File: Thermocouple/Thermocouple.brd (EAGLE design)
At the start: 25.4 x 25.4 mm, 20 parts, among them Q2 BSS138

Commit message: Latest version of schematics and boards
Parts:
- removed C5: 10uF, SparkFun-Capacitors:0805
- removed LED: blue, led:CHIPLED_1206
- removed Q2: BSS138, SparkFun-DiscreteSemi:SOT23
- added C10, C4: 1uF, SparkFun-Capacitors:0805
- added C12, C6, C8, C9: .1uF, SparkFun-Capacitors:0805
- added C7: .47uF, SparkFun-Capacitors:0805
- added JP2: M023.5MM, SparkFun-Connectors:SCREWTERMINAL-3.5MM-2
- added L1: 1mH, SparkFun-Passives:1007
- added LED1: (no value), adafruit:CHIP-LED0805
- added R4: 24k, SparkFun-Resistors:0805
- added TP1, TP2, TP3, TP4, TP5, TP6, TP7, TP8, TP9: TEST-POINT3, SparkFun-Passives:PAD.03X.03
- C1: value .1uF -> .47uF
- C2: value 10uF -> .1uF
- JP1: value (none) -> M023.5MM; device SparkFun-Connectors:SCREWTERMINAL-3.5MM-4 -> SparkFun-Connectors:SCREWTERMINAL-3.5MM-2
- R1: value 1k -> 680; device SparkFun-Resistors:0805 -> SparkFun-Passives:0805
- R2: value 2k -> 1
- R3: value 680 -> 24k; device SparkFun-Passives:0805 -> SparkFun-Resistors:0805
- R5, R8: value 1k -> 1M
- R6: value 2k -> 24k
- R7: value 1k -> 24k
- R9: value 2k -> 22; device SparkFun-Resistors:0805 -> SparkFun-Passives:0805
- U$1: value MAX31855 -> AD8495; device IntegerLabs:SOIC-8 -> IntegerLabs:MSOP-8
- U$2: value MIC5205-3.3 -> FOOTPRINTFOOTPRINT-2; device SparkFun-PowerIC:SOT23-5 -> IntegerLabs:FOOTPRINT2
- U$3: value TINY841 -> ATTINY48/88-TQFP; device IntegerLabs:SOIC14 -> IntegerLabs:TQFP-32
- U$4: value FOOTPRINT -> AD8495; device IntegerLabs:FOOTPRINT -> IntegerLabs:MSOP-8
- U$5: value MAX31855 -> zener; device IntegerLabs:SOIC-8 -> SparkFun-DiscreteSemi:SOD-323
- moved R3 28.3 mm to (31.1, 12.4), turned to 90 degrees
- moved U$4 28.1 mm to (19.7, 20.0), turned to 90 degrees
- moved C2 24.5 mm to (27.3, 15.6), turned to 270 degrees
- moved R5 14.5 mm to (29.2, 12.4), turned to 270 degrees
- moved R6 13.9 mm to (22.9, 12.1), turned to 90 degrees
- moved U$5 13.7 mm to (17.1, 24.1), turned to 270 degrees
- moved C3 13.6 mm to (31.1, 15.6)
- moved JP1 13.3 mm to (22.5, 6.67)
- moved U$2 13.0 mm to (0.00, 0.00), turned to 0 degrees
- moved U$1 11.5 mm to (28.6, 20.3), turned to 90 degrees
- moved R8 10.4 mm to (21.0, 12.1), turned to 270 degrees
- moved R1 9.38 mm to (22.5, 27.9), turned to 90 degrees
- moved R9 9.14 mm to (19.4, 24.1), turned to 90 degrees
- moved U$3 7.96 mm to (8.57, 21.3)
- moved R7 7.81 mm to (19.1, 12.1), turned to 90 degrees
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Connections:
- removed net +3.3V: C3.1, C5.1, U$1.4, U$2.5, U$5.4
- removed net +5V: C1.1, C2.1, R1.2, U$2.1, U$2.3, U$3.1, U$4.P$1
- removed net CS1: R2.2, U$3.2
- removed net CS1-3.3: R2.1, R5.2, U$1.6
- removed net CS2: R6.2, U$3.3
- removed net CS2-3.3: R6.1, R7.2, U$5.6
- removed net MISO3.3: Q2.1, U$1.7, U$5.7
- removed net MISO5: Q2.3, R1.1, U$3.6
- removed net SCK-3.3: R8.2, R9.1, U$1.5, U$5.5
- removed net SCL/SCK: U$3.9, U$4.P$4
- removed net SDA/MOSI: U$3.7, U$4.P$2
- removed net T1+: JP1.4, U$1.3
- removed net T1-: JP1.3, U$1.2
- removed net T2+: JP1.2, U$5.3
- removed net T2-: JP1.1, U$5.2
- new net AVCC: C7.1, L1.1, TP4.P$1, TP5.P$1, U$1.7, U$3.18, U$4.7, U$5.1
- new net IN1+: JP1.1, R4.1, TP6.P$1
- new net IN1-: JP1.2, R3.1, R5.2, TP7.P$1
- new net IN2+: JP2.1, R7.1, TP8.P$1
- new net IN2-: JP2.2, R6.1, R8.2, TP9.P$1
- new net MOSI: U$2.PROG4, U$3.15
- new net N$2: R2.2, U$2.BUS2
- new net N$3: C3.2, C4.1, R3.2, U$1.1
- new net N$4: C2.1, C4.2, R4.2, U$1.8
- new net N$6: C10.2, C8.1, R7.2, U$4.8
- new net N$7: L1.2, R9.1
- new net N$8: LED1.A, R1.1
- new net SCL: U$2.BUS3, U$3.28
- new net SDA: U$2.BUS1, U$3.27
- new net TEMP1: C6.1, TP1.P$1, U$1.5, U$1.6, U$3.3
- new net TEMP2: C12.1, TP2.P$1, U$3.6, U$4.5, U$4.6
- new net VCC: C1.2, R2.1, R9.2, U$2.PROG0, U$3.4
- net GND: now also C1.1, C12.2, C3.1, C6.2, C7.2, C8.2, C9.1, LED1.C, TP3.P$1, U$1.2, U$1.3, U$2.BUS0, U$3.21, U$3.5, U$4.2, U$4.3, U$5.2; no longer C1.2, C3.2, C5.2, LED.C, Q2.2, R7.1, U$1.1, U$2.2, U$3.14, U$4.P$3, U$5.1
- net LED: now also R1.2, U$3.13; no longer R3.2, U$3.12
- net MISO: now also U$2.PROG3, U$3.16; no longer U$3.8, U$4.MISO
- net N$5: now also C10.1, C9.2, R6.2, U$4.1; no longer LED.A, R3.1
- net RESET: now also U$2.PROG1, U$3.29; no longer U$3.4, U$4.RESET
- net SCK: now also U$2.PROG2, U$3.17; no longer R9.2, U$3.5
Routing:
- net VCC: track 0.00 -> 40.9 mm, vias 0 -> 1
- net TEMP1: track 0.00 -> 39.0 mm, vias 0 -> 5
- net +5V: track 37.7 -> 0.00 mm, vias 3 -> 0
- net GND: track 72.3 -> 38.8 mm, vias 5 -> 14
- net AVCC: track 0.00 -> 32.3 mm
- net SCL: track 0.00 -> 25.0 mm, vias 0 -> 1
- net SCK-3.3: track 21.9 -> 0.00 mm, vias 4 -> 0
- net LED: track 10.4 -> 31.9 mm, vias 0 -> 2
- net +3.3V: track 21.2 -> 0.00 mm
- net MOSI: track 0.00 -> 19.5 mm, vias 0 -> 1
- net SCL/SCK: track 19.1 -> 0.00 mm, vias 1 -> 0
- net MISO5: track 18.0 -> 0.00 mm, vias 2 -> 0
- net IN2-: track 0.00 -> 17.9 mm
- net MISO3.3: track 17.2 -> 0.00 mm
- net IN1+: track 0.00 -> 16.1 mm
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- added copper zone on layer 16, net GND
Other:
- board size 25.4 x 25.4 mm -> 35.6 x 29.8 mm
- board text added: "+: yellow"
- board text added: "-"
- board text added: "-: red"
- board text added: "A"
- board text added: "A+"
- board text added: "A-"
- board text added: "B"
- board text added: "B+"
- board text added: "B-"
- board text added: "Modulo"
- board text added: "Thermocouple"
- board text added: "v3 2014-10-10"
- board text removed: "2014-07-03"
- board text removed: "T1+"
- board text removed: "T1-"
- board text removed: "T2+"
- board text removed: "T2-"
- board text removed: "Thermocouple v1"

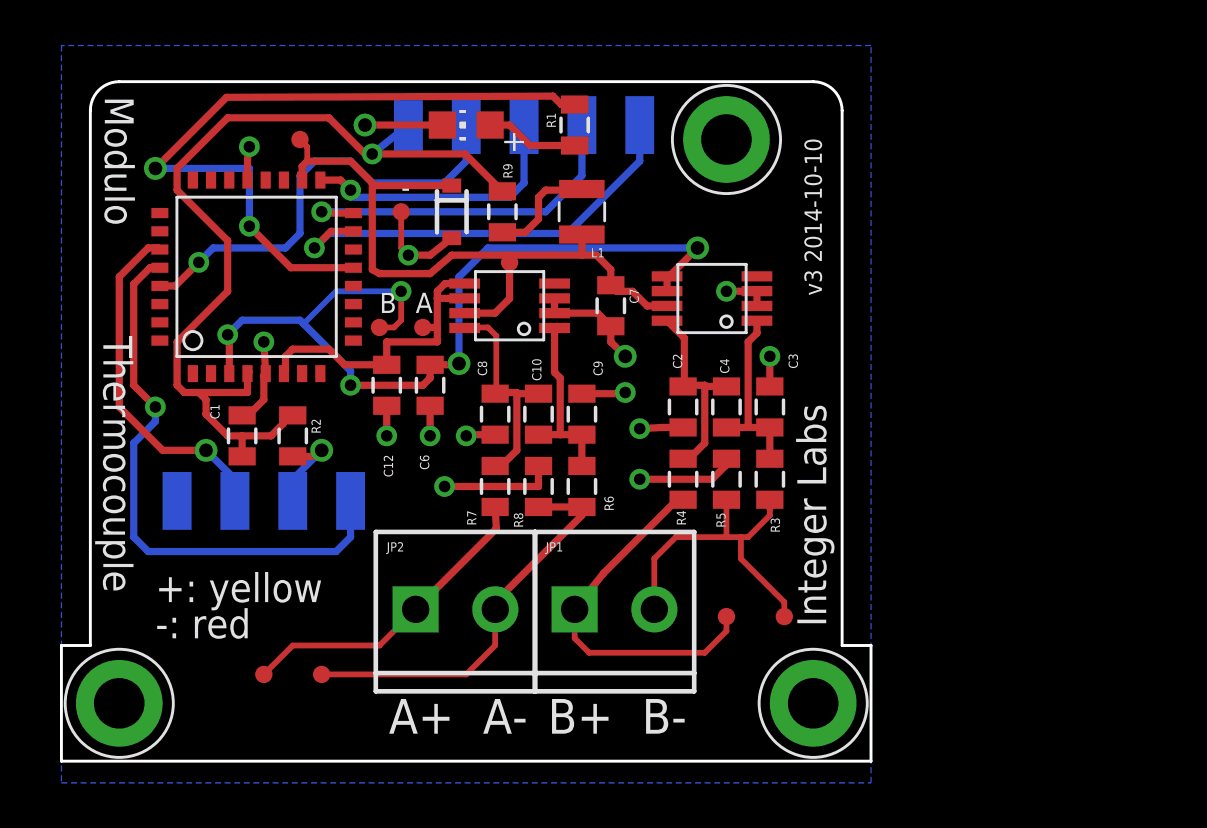
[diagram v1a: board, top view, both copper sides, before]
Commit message: OLED: added buttons and rewired for attiny841 Thermocouple: checkpoint of latest version with two amplifiers and attiny48
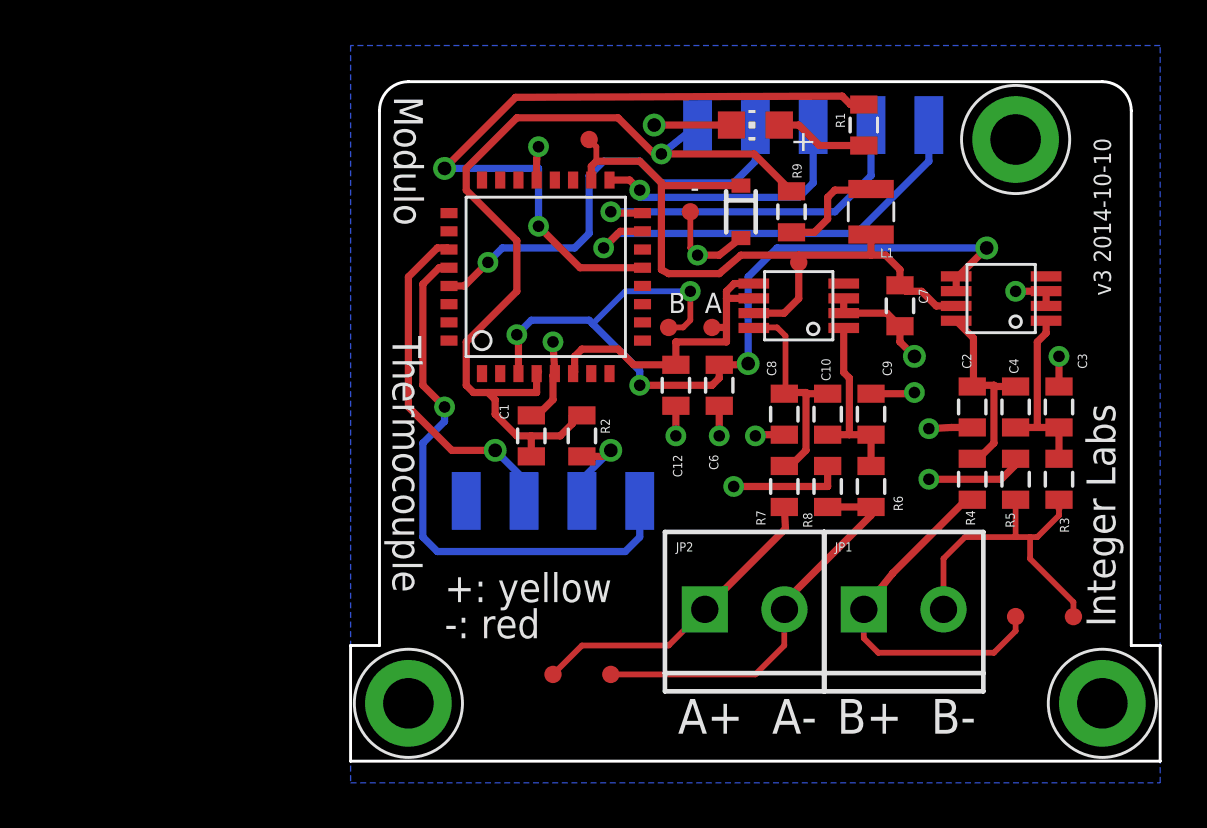
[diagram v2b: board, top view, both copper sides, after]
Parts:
- moved C10 12.7 mm to (33.7, 15.2)
- moved C2 12.7 mm to (40.0, 15.6)
- moved C9 12.7 mm to (35.6, 15.2)
- moved L1 12.7 mm to (35.6, 24.1)
- moved R4 12.7 mm to (40.0, 12.4)
- moved R6 12.7 mm to (35.6, 12.1)
- moved R8 12.7 mm to (33.7, 12.1)
- moved R9 12.7 mm to (32.1, 24.1)
- moved TP7 12.7 mm to (44.5, 6.35)
- moved C12 12.7 mm to (27.0, 16.5)
- moved JP2 12.7 mm to (28.3, 6.67)
- moved TP1 12.7 mm to (26.7, 19.1)
- moved U$3 12.7 mm to (21.3, 21.3)
- moved C1 12.7 mm to (20.6, 14.3)
- moved C3 12.7 mm to (43.8, 15.6)
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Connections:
- net TEMP1 renamed TEMPB
- net TEMP2 renamed TEMPA

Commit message: New thermocouple revision with single input and quick connect terminals
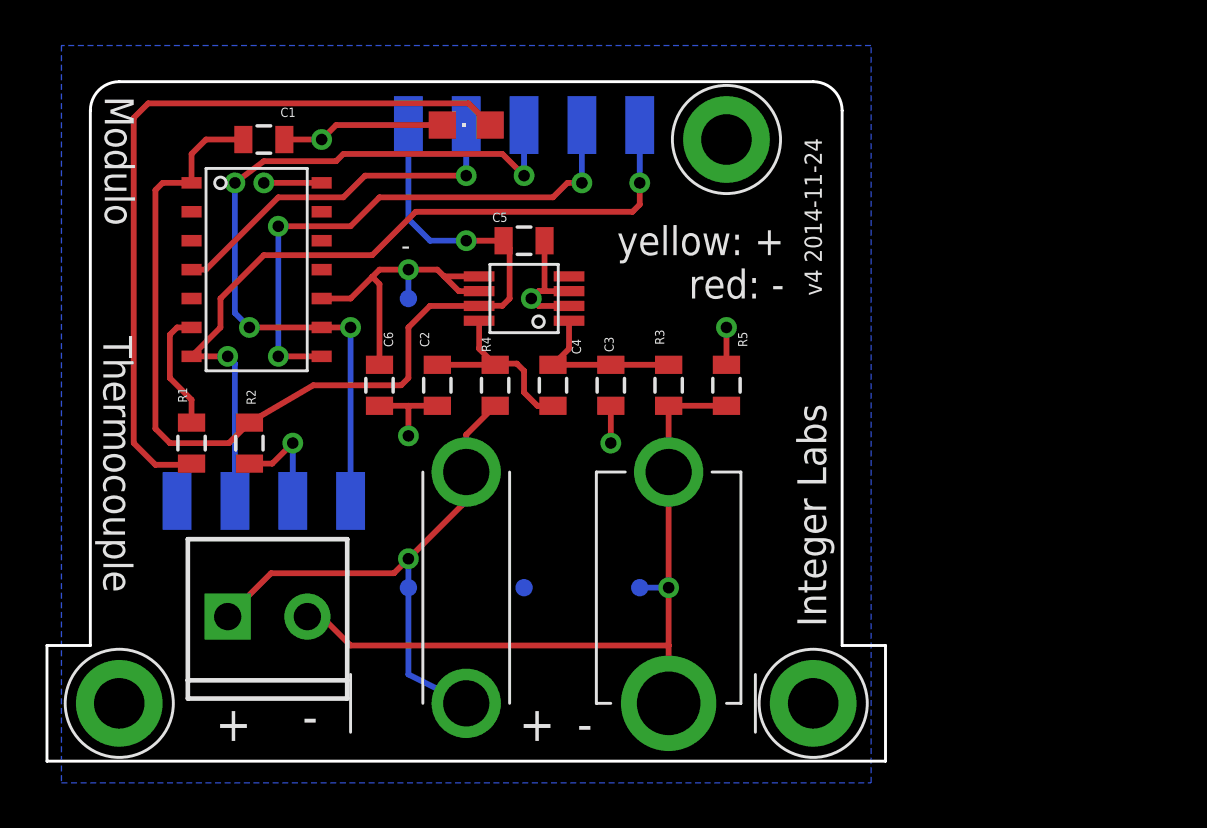
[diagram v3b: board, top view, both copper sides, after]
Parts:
- removed C10: 1uF, SparkFun-Capacitors:0805
- removed C12, C8, C9: .1uF, SparkFun-Capacitors:0805
- removed C7: .47uF, SparkFun-Capacitors:0805
- removed JP2: M023.5MM, SparkFun-Connectors:SCREWTERMINAL-3.5MM-2
- removed L1: 1mH, SparkFun-Passives:1007
- removed R6, R7: 24k, SparkFun-Resistors:0805
- removed R8: 1M, SparkFun-Resistors:0805
- removed R9: 22, SparkFun-Passives:0805
- removed TP1, TP4, TP5, TP8, TP9: TEST-POINT3, SparkFun-Passives:PAD.03X.03
- removed U$5: zener, SparkFun-DiscreteSemi:SOD-323
- added C5: .47uF, SparkFun-Capacitors:0805
- C2, C3, C6: value .1uF -> .47uF
- LED1: device adafruit:CHIP-LED0805 -> adafruit:CHIPLED_0805
- U$3: value ATTINY48/88-TQFP -> TINY841; device IntegerLabs:TQFP-32 -> IntegerLabs:SOIC14
- U$4: value AD8495 -> THERMOCOUPLE-JACK; device IntegerLabs:MSOP-8 -> IntegerLabs:THERMOCOUPLE-JACK
- moved R1 32.7 mm to (5.71, 14.0)
- moved JP1 27.9 mm to (7.30, 6.35)
- moved TP6 26.7 mm to (15.2, 7.62), flipped to the bottom
- moved C2 23.5 mm to (16.5, 16.5)
- moved U$4 22.8 mm to (17.8, 2.54), turned to 0 degrees
- moved R4 21.4 mm to (19.1, 16.5)
- moved U$1 21.0 mm to (20.3, 20.3)
- moved C4 20.3 mm to (21.6, 16.5), turned to 270 degrees
- moved C3 19.7 mm to (24.1, 16.5), turned to 90 degrees
- moved TP7 19.1 mm to (25.4, 7.62), flipped to the bottom
- moved TP3 18.1 mm to (20.3, 7.62), flipped to the bottom
- moved R3 17.6 mm to (26.7, 16.5)
- moved C1 17.5 mm to (8.89, 27.3), turned to 180 degrees
- moved C6 14.9 mm to (14.0, 16.5)
- moved R2 14.6 mm to (8.26, 14.0)
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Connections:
- removed net AVCC: C7.1, L1.1, TP4.P$1, TP5.P$1, U$1.7, U$3.18, U$4.7, U$5.1
- removed net IN2+: JP2.1, R7.1, TP8.P$1
- removed net IN2-: JP2.2, R6.1, R8.2, TP9.P$1
- removed net MOSI: U$2.PROG4, U$3.15
- removed net N$5: C10.1, C9.2, R6.2, U$4.1
- removed net N$6: C10.2, C8.1, R7.2, U$4.8
- removed net N$7: L1.2, R9.1
- removed net SCK: U$2.PROG2, U$3.17
- removed net SCL: U$2.BUS3, U$3.28
- removed net SDA: U$2.BUS1, U$3.27
- removed net TEMPA: C12.1, TP2.P$1, U$3.6, U$4.5, U$4.6
- removed net TEMPB: C6.1, TP1.P$1, U$1.5, U$1.6, U$3.3
- new net SCL/SCK: U$2.BUS3, U$2.PROG2, U$3.9
- new net SDA/MOSI: U$2.BUS1, U$2.PROG4, U$3.7
- new net TEMP: C6.1, TP2.P$1, U$1.5, U$1.6, U$3.10
- net GND: now also C5.2, U$3.14; no longer C12.2, C7.2, C8.2, C9.1, R8.1, U$3.21, U$3.5, U$4.2, U$4.3, U$5.2
- net IN1+: now also U$4.POS1, U$4.POS2
- net IN1-: now also U$4.NEG1, U$4.NEG2
- net LED: now also U$3.6; no longer U$3.13
- net MISO: now also U$3.8; no longer U$3.16
- net RESET: now also U$3.4; no longer U$3.29
- net VCC: now also C5.1, U$1.7, U$3.1; no longer R9.2, U$3.4
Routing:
- net TEMPB: track 39.0 -> 0.00 mm, vias 5 -> 0
- net SDA/MOSI: track 0.00 -> 34.8 mm, vias 0 -> 2
- net SCL/SCK: track 0.00 -> 34.4 mm, vias 0 -> 4
- net AVCC: track 32.3 -> 0.00 mm
- net N$8: track 4.09 -> 33.6 mm
- net LED: track 31.9 -> 5.34 mm, vias 2 -> 0
- net SCL: track 25.0 -> 0.00 mm, vias 1 -> 0
- net MOSI: track 19.5 -> 0.00 mm, vias 1 -> 0
- net IN1-: track 15.1 -> 33.3 mm, vias 0 -> 1
- net IN2-: track 17.9 -> 0.00 mm
- net GND: track 38.8 -> 22.7 mm, vias 14 -> 6
- net SDA: track 15.4 -> 0.00 mm, vias 1 -> 0
- net TEMP: track 0.00 -> 14.6 mm, vias 0 -> 1
- net TEMPA: track 14.3 -> 0.00 mm
- net IN2+: track 13.8 -> 0.00 mm
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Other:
- board size 35.6 x 29.8 mm -> 36.8 x 29.8 mm
- board text added: "+"
- board text added: "red: -"
- board text added: "v4 2014-11-24"
- board text added: "yellow: +"
- board text removed: "+: yellow"
- board text removed: "-: red"
- board text removed: "A"
- board text removed: "A+"
- board text removed: "A-"
- board text removed: "B"
- board text removed: "B+"
- board text removed: "B-"
- board text removed: "v3 2014-10-10"

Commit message: New versions of IntegerLabs library, RotaryEncoder, and Thermocouple
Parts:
- LED1: device adafruit:CHIPLED_0805 -> adafruit:CHIP-LED0805
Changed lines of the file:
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@@
 </element>
 <element name="U$2" library="IntegerLabs" package="FOOTPRINT2" value="FOOTPRINTFOOTPRINT-2" x="0" y="0"/>
-<element name="LED1" library="adafruit" package="CHIPLED_0805" value="" x="17.78" y="27.94" smashed="yes" rot="R90">
+<element name="LED1" library="adafruit" package="CHIP-LED0805" value="" x="17.78" y="27.94" smashed="yes" rot="R90">
 <attribute name="VALUE" x="19.05" y="30.48" size="1.27" layer="27" rot="R180"/>
 </element>

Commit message: Checkpointing PCB designs
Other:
- board size 36.8 x 29.8 mm -> 36.3 x 29.8 mm
- board text removed: "Integer Labs"
- board text removed: "Modulo"
- board text removed: "Thermocouple"
- board text removed: "v4 2014-11-24"
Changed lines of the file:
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@@
 <layers>
 <layer number="1" name="Top" color="4" fill="1" visible="yes" active="yes"/>
+<layer number="2" name="Route2" color="1" fill="3" visible="yes" active="yes"/>
+<layer number="3" name="Route3" color="4" fill="3" visible="no" active="yes"/>
+<layer number="14" name="Route14" color="1" fill="6" visible="no" active="yes"/>
+<layer number="15" name="Route15" color="4" fill="6" visible="no" active="yes"/>
 <layer number="16" name="Bottom" color="1" fill="1" visible="yes" active="yes"/>
 <layer number="17" name="Pads" color="2" fill="1" visible="yes" active="yes"/>
@@
 <board>
 <plain>
-<text x="33.5915" y="5.9055" size="1.27" layer="21" font="vector" ratio="12" rot="R90">Integer Labs</text>
-<text x="1.8415" y="18.669" size="1.27" layer="21" font="vector" ratio="12" rot="SR270">Thermocouple</text>
-<text x="33.401" y="20.447" size="0.762" layer="21" font="vector" ratio="10" rot="R90">v4 2014-11-24</text>
 <text x="10.922" y="1.2065" size="1.524" layer="21" font="vector" ratio="12" align="bottom-center">-</text>
 <text x="7.5565" y="0.889" size="1.524" layer="21" font="vector" ratio="12" align="bottom-center">+</text>
-<text x="1.905" y="29.21" size="1.27" layer="21" font="vector" ratio="12" rot="SR270">Modulo</text>
 <text x="31.75" y="20.955" size="1.27" layer="21" font="vector" ratio="12" align="center-right">red: -</text>
 <text x="31.75" y="22.86" size="1.27" layer="21" font="vector" ratio="12" align="center-right">yellow: +</text>
@@
 <attribute name="VALUE" x="5.842" y="11.3665" size="0.4064" layer="27" font="vector" rot="R90"/>
 </element>
-<element name="U$2" library="IntegerLabs" package="FOOTPRINT2" value="FOOTPRINTFOOTPRINT-2" x="0" y="0"/>
+<element name="U$2" library="IntegerLabs" package="FOOTPRINT2" value="FOOTPRINTFOOTPRINT-2" x="0" y="0">
+<attribute name="VERSION" value="v5" x="0" y="0" size="1.778" layer="27" display="off"/>
+<attribute name="BOARD" value="Thermocouple" x="0" y="0" size="1.778" layer="27" display="off"/>
+</element>
 <element name="LED1" library="adafruit" package="CHIP-LED0805" value="" x="17.78" y="27.94" smashed="yes" rot="R90">
 <attribute name="VALUE" x="19.05" y="30.48" size="1.27" layer="27" rot="R180"/>

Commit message: Various updates
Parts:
- removed R2: 1, SparkFun-Resistors:0805
- removed TP2, TP3, TP6, TP7: TEST-POINT3, SparkFun-Passives:PAD.03X.03
- removed U$2: FOOTPRINTFOOTPRINT-2, IntegerLabs:FOOTPRINT2
- removed U$3: TINY841, IntegerLabs:SOIC14
- added U1: ATTINY841, Modulo:SOIC-14
- added U2: EXCLUDE, Modulo:DEVICE-PCB
- C1, C2, C3, C5, C6: value .47uF -> 100nF; device SparkFun-Capacitors:0805 -> Modulo:0603
- C4: device SparkFun-Capacitors:0805 -> Modulo:0603
- LED1: value (none) -> blue; device adafruit:CHIP-LED0805 -> Modulo:0805-LED
- R1: value 680 -> 681Ω; device SparkFun-Passives:0805 -> Modulo:0603
- R3, R4, R5: device SparkFun-Resistors:0805 -> Modulo:0603
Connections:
- removed net N$2: R2.2, U$2.BUS2
- net GND: now also U1.14, U2.BUS0; no longer TP3.P$1, U$2.BUS0, U$3.14
- net IN1+: no longer TP6.P$1
- net IN1-: no longer TP7.P$1
- net LED: now also U1.6; no longer U$3.6
- net MISO: now also U1.8, U2.PROG3; no longer U$2.PROG3, U$3.8
- net RESET: now also U1.4, U2.PROG1; no longer U$2.PROG1, U$3.4
- net SCL/SCK: now also U1.9, U2.BUS3, U2.PROG2; no longer U$2.BUS3, U$2.PROG2, U$3.9
- net SDA/MOSI: now also U1.7, U2.BUS1, U2.PROG4; no longer U$2.BUS1, U$2.PROG4, U$3.7
- net TEMP: now also U1.10; no longer TP2.P$1, U$3.10
- net VCC: now also U1.1, U2.BUS2, U2.PROG0; no longer R2.1, U$2.PROG0, U$3.1
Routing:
- net SCL/SCK: track 34.4 -> 23.2 mm, vias 4 -> 1
- net N$2: track 4.82 -> 0.00 mm, vias 1 -> 0
- net VCC: track 46.9 -> 51.2 mm, vias 1 -> 2
- net GND: track 22.7 -> 25.6 mm, vias 6 -> 5
- net SDA/MOSI: track 34.8 -> 33.4 mm
- net IN1-: track 33.3 -> 32.2 mm
- net TEMP: track 14.6 -> 13.5 mm
